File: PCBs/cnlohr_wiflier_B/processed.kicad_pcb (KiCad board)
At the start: 2 copper layers, 37.8 x 21.5 mm, 61 parts, among them CN1 10p, J1 AVRISP6, P1 WS2812, P10 SCL, P11 3V, P12 GND, P13 LED, P14 LED, P15 GND, P16 FLTBAT, P17 TOUT, P18 AVRA0, P2 M0, P21 B+, P24 B-, P3 M1, P32 ESP_UART, P4 M2, P5 M3, P6 ANT, P9 SDA, Q1 7A_20V, Q2 7A_20V, Q3 7A_20V, Q4 7A_20V, U1 MCP1824/3.3, U2 MCP1824/3.3, U3 BMP280, U4 LSM9DS1, U5 ESP8266EX, U6 W25Q80DV, U7 ATTINY441-QFN, X1 26MHz

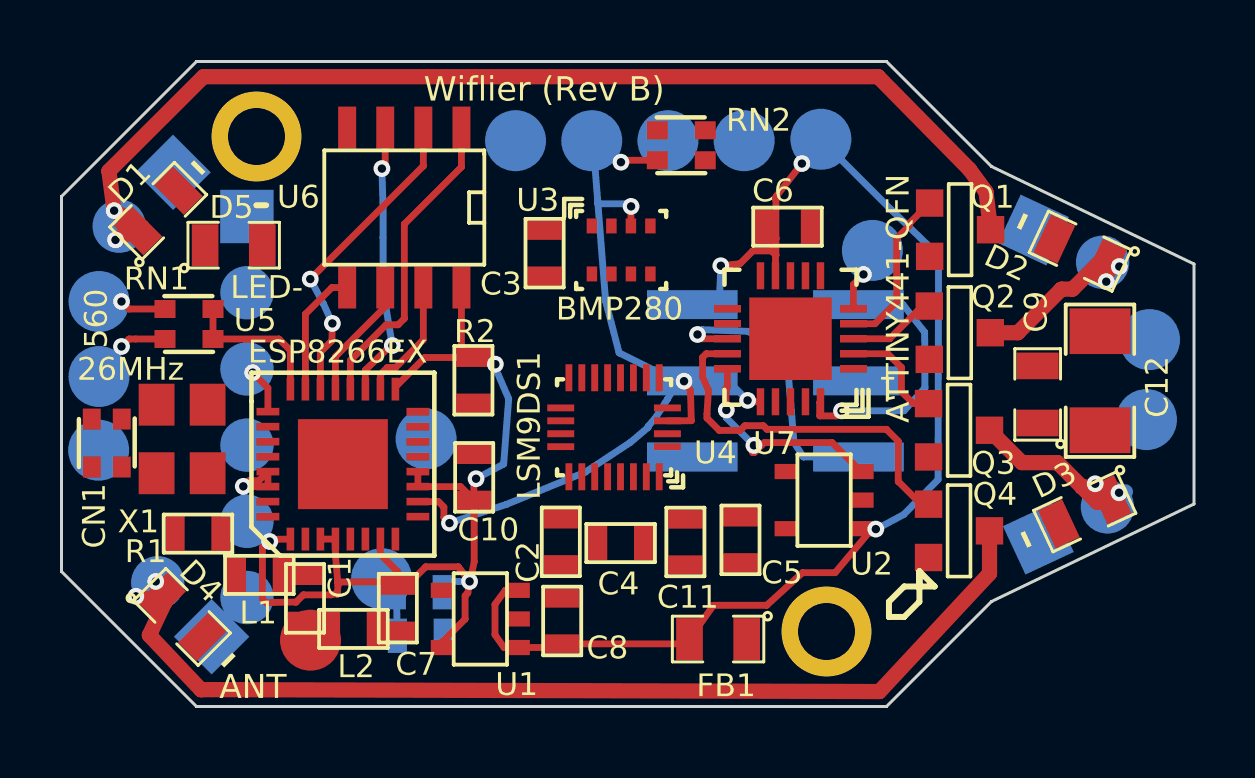
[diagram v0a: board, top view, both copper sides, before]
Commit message: recheck all circuits and clean up fill zone by rerouting the nets using freerouting and manually
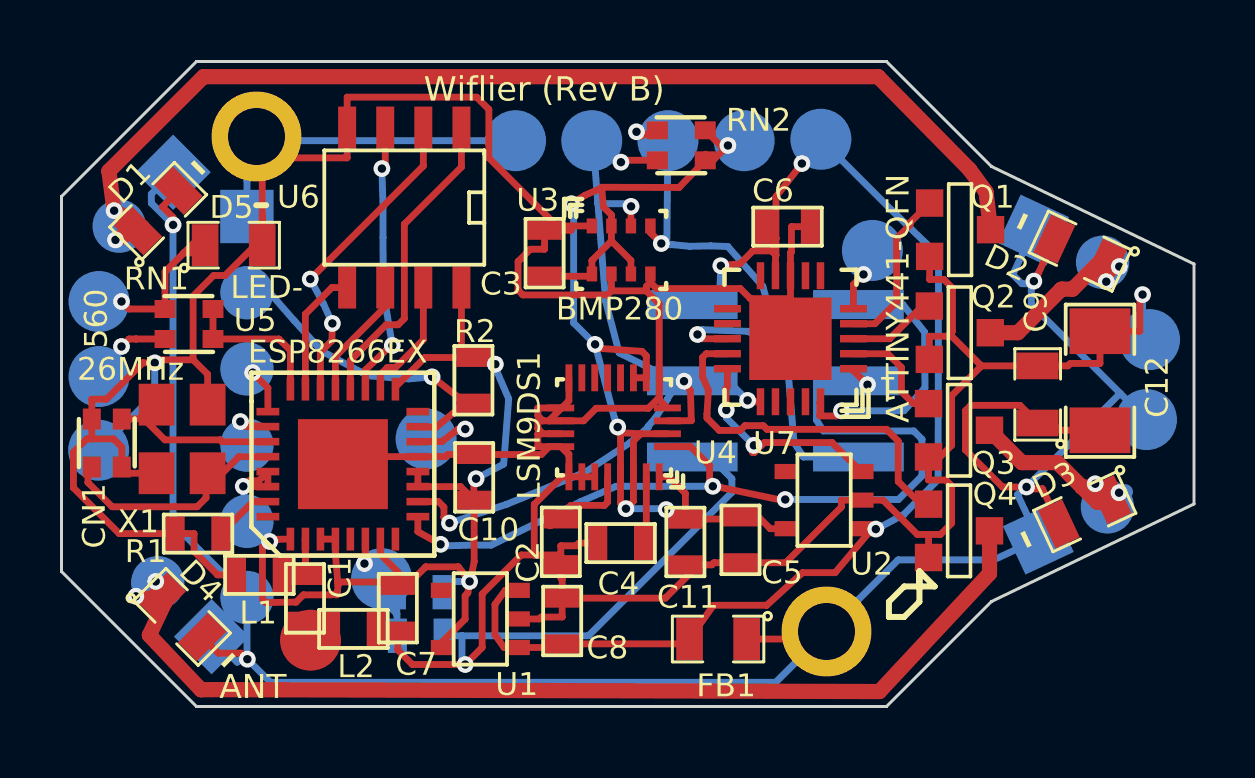
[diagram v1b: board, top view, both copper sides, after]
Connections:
- C10 pad 2: (no net) -> GND
- C11 pad 1: (no net) -> +3.3VP
- C11 pad 2: (no net) -> GND
- C12 pad 1: (no net) -> +BATT
- C12 pad 2: (no net) -> GND
- C2 pad 1: (no net) -> GND
- C2 pad 2: (no net) -> N-0000037
- C3 pad 1: (no net) -> +3.3VP
- C3 pad 2: (no net) -> GND
- C4 pad 1: (no net) -> GND
- C4 pad 2: (no net) -> N-0000040
- C5 pad 1: (no net) -> +3.3VP
- C5 pad 2: (no net) -> GND
- C6 pad 1: (no net) -> GND
- C7 pad 2: (no net) -> GND
- C8 pad 2: (no net) -> GND
- C9 pad 1: (no net) -> +BATT
- C9 pad 2: (no net) -> GND
- CN1 pad 1: (no net) -> N-0000015
- CN1 pad 2: (no net) -> GND
- CN1 pad 3: (no net) -> GND
- CN1 pad 4: (no net) -> N-0000019
- D1 pad 1: (no net) -> M0P
- D1 pad 2: (no net) -> +BATT
- D2 pad 1: (no net) -> M1P
- D2 pad 2: (no net) -> +BATT
- D3 pad 1: (no net) -> M2P
- D3 pad 2: (no net) -> +BATT
- D4 pad 1: (no net) -> M3P
- D4 pad 2: (no net) -> +BATT
- D5 pad 1: (no net) -> N-0000023
- D5 pad 2: (no net) -> GND
- FB1 pad 1: (no net) -> +BATT
- J1 pad 3: (no net) -> SCL
- J1 pad 4: (no net) -> SDA
- J1 pad 6: (no net) -> GND
- L1 pad 2: (no net) -> GND
- L2 pad 2: (no net) -> GND
- P1 pad 1: (no net) -> GPIO2
- P10 pad 1: (no net) -> SCL
- P11 pad 1: (no net) -> +3.3VP
- P12 pad 1: (no net) -> GND
- P15 pad 1: (no net) -> GND
- P17 pad 1: (no net) -> TOUT
- P2 pad 1: (no net) -> +BATT
- P2 pad 2: (no net) -> M0P
- P21 pad 1: (no net) -> +BATT
- P24 pad 1: (no net) -> GND
- P3 pad 1: (no net) -> +BATT
- P3 pad 2: (no net) -> M1P
- P32 pad 1: (no net) -> GND
- P32 pad 2: (no net) -> GPIO0
- P32 pad 4: (no net) -> UTX
- P32 pad 5: (no net) -> +3.3V
- P32 pad 6: (no net) -> +BATT
- P4 pad 1: (no net) -> +BATT
- P4 pad 2: (no net) -> M2P
- P5 pad 1: (no net) -> +BATT
- P5 pad 2: (no net) -> M3P
- P6 pad 1: (no net) -> N-0000026
- P7 pad 1: (no net) -> GND
- P8 pad 1: (no net) -> +BATT
- Q1 pad S: (no net) -> GND
- Q2 pad S: (no net) -> GND
- Q3 pad S: (no net) -> GND
- Q4 pad S: (no net) -> GND
- R1 pad 1: (no net) -> GND
- R1 pad 2: (no net) -> N-0000021
- R2 pad 1: (no net) -> GPIO0
- R2 pad 2: (no net) -> +3.3V
- R5 pad 2: (no net) -> GND
- RN2 pad 1: (no net) -> +3.3VP
- RN2 pad 3: (no net) -> +3.3VP
- RN2 pad 4: (no net) -> SCL
- U1 pad 2: (no net) -> GND
- U2 pad 2: (no net) -> GND
- U2 pad 5: (no net) -> +3.3VP
- U3 pad 1: (no net) -> GND
- U3 pad 2: (no net) -> +3.3VP
- U3 pad 4: (no net) -> SCL
- U3 pad 5: (no net) -> GND
- U3 pad 6: (no net) -> +3.3VP
- U3 pad 7: (no net) -> GND
- U3 pad 8: (no net) -> +3.3VP
- U4 pad 1: (no net) -> +3.3VP
- U4 pad 13: (no net) -> GND
- U4 pad 14: (no net) -> GND
- U4 pad 15: (no net) -> GND
- U4 pad 16: (no net) -> GND
- U4 pad 17: (no net) -> GND
- U4 pad 18: (no net) -> GND
- U4 pad 19: (no net) -> GND
- U4 pad 2: (no net) -> SCL
- U4 pad 20: (no net) -> GND
- U4 pad 21: (no net) -> N-0000037
- U4 pad 22: (no net) -> +3.3VP
- U4 pad 23: (no net) -> +3.3VP
- U4 pad 24: (no net) -> N-0000040
- U4 pad 3: (no net) -> +3.3VP
- U4 pad 5: (no net) -> GND
- U4 pad 6: (no net) -> GND
- U4 pad 7: (no net) -> +3.3VP
- U4 pad 8: (no net) -> +3.3VP
- U5 pad 13: (no net) -> GND
- U5 pad 14: (no net) -> GPIO2
- U5 pad 15: (no net) -> GPIO0
- U5 pad 2: (no net) -> N-000004
- U5 pad 26: (no net) -> UTX
- U5 pad 27: (no net) -> N-0000019
- U5 pad 28: (no net) -> N-0000015
- U5 pad 31: (no net) -> N-0000021
- U5 pad 33: (no net) -> GND
- U5 pad 6: (no net) -> TOUT
- U5 pad 9: (no net) -> SCL
- U6 pad 4: (no net) -> GND
- U7 pad 1: (no net) -> SCL
- U7 pad 21: (no net) -> GND
- U7 pad 8: (no net) -> GND
- X1 pad 1: (no net) -> N-0000019
- X1 pad 2: (no net) -> N-0000015
- X1 pad 3: (no net) -> GND
- X1 pad 4: (no net) -> GND
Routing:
- net GND: track 0.00 -> 172.6 mm, vias 0 -> 3
- net +BATT: track 0.00 -> 81.3 mm, vias 0 -> 4
- net SCL: track 0.00 -> 44.5 mm, vias 0 -> 6
- net +3.3VP: track 0.00 -> 39.9 mm, vias 0 -> 6
- net GPIO0: track 0.00 -> 10.9 mm, vias 0 -> 1
- net N-0000015: track 0.00 -> 8.89 mm
- net N-0000019: track 0.00 -> 6.52 mm
- net N-0000023: track 2.30 -> 6.08 mm
- net UTX: track 0.00 -> 3.43 mm, vias 0 -> 1
- net N-0000037: track 0.00 -> 3.19 mm
- net GPIO2: track 0.00 -> 3.18 mm, vias 0 -> 1
- net TOUT: track 1.45 -> 4.64 mm, vias 0 -> 1
- net N-0000040: track 0.00 -> 2.25 mm
- net N-0000021: track 0.00 -> 2.16 mm
- net N-000004: track 0.77 -> 2.08 mm
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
